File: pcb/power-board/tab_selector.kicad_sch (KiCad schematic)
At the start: 4 parts, among them K20 FINDER-40.41, K21 FINDER-40.41

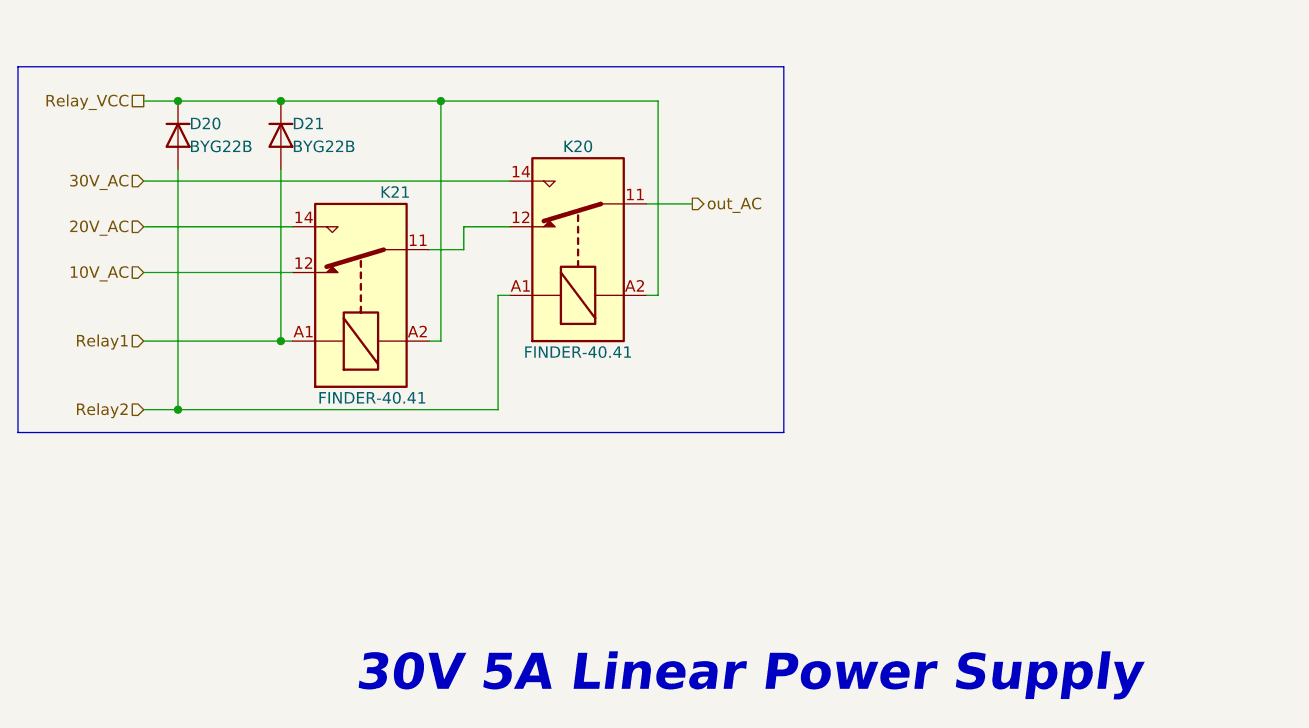
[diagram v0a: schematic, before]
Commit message: Perform minor stylistic changes on power-board schematic, clear DRC
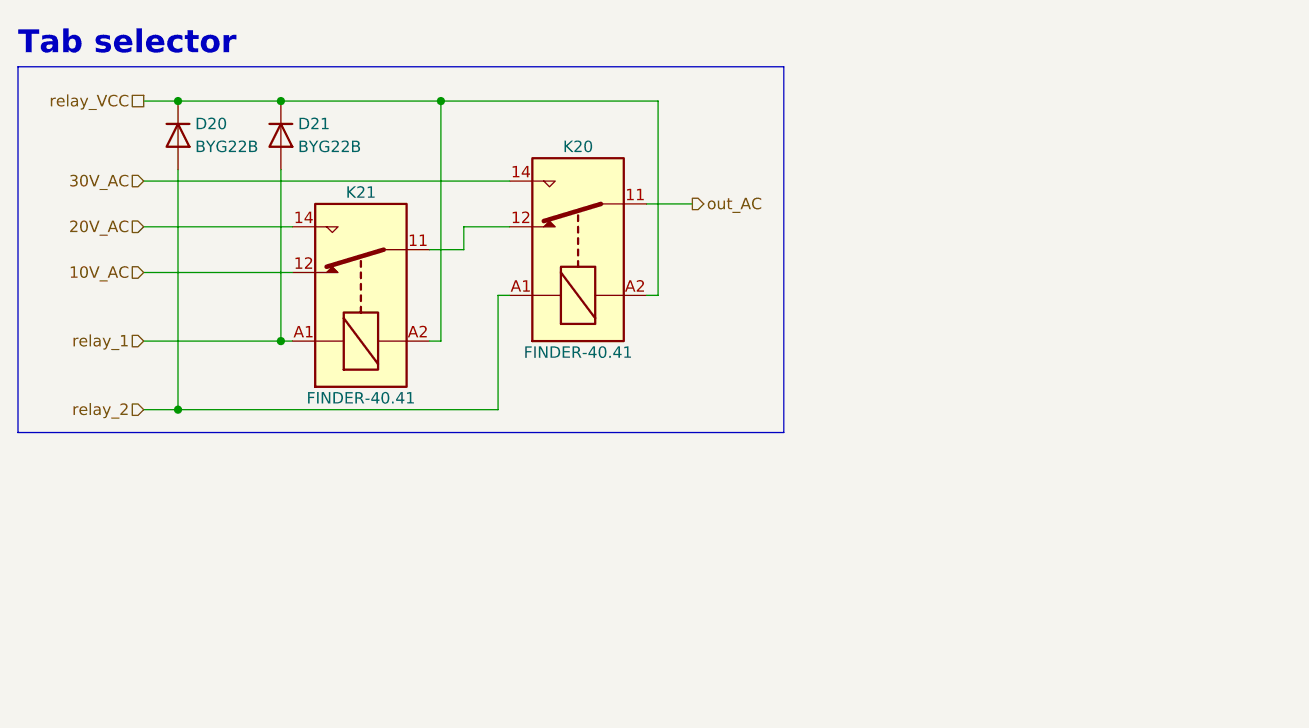
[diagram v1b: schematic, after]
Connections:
- net Relay1 renamed relay_1
- net Relay2 renamed relay_2
- net Relay_VCC renamed relay_VCC
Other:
- note added: "Tab selector"
- note removed: "30V 5A Linear Power Supply"
- title: Tab selector -> DW3005T-power-board
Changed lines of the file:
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@@
 	(paper "A5")
 	(title_block
-		(title "Tab selector")
-		(date "2024-02-24")
-		(rev "V1.0")
+		(title "DW3005T-power-board")
+		(date "2024-02-26")
+		(rev "1.0.0")
 		(company "Dominik Workshop")
 	)
@@
 		)
 	)
-	(text "30V 5A Linear Power Supply"
+	(text "Tab selector"
 		(exclude_from_sim no)
-		(at 95.885 114.3 0)
-		(effects
-			(font
-				(size 4 4)
-				(thickness 0.8)
+		(at 58.42 41.91 0)
+		(effects
+			(font
+				(size 2.54 2.54)
+				(thickness 0.508)
 				(bold yes)
-				(italic yes)
-			)
-			(justify left bottom)
+			)
+			(justify left)
 		)
 	)
@@
 		)
 	)
-	(hierarchical_label "Relay_VCC"
+	(hierarchical_label "relay_VCC"
 		(shape passive)
 		(at 72.39 48.26 180)
@@
 		)
 	)
-	(hierarchical_label "Relay2"
+	(hierarchical_label "relay_2"
 		(shape input)
 		(at 72.39 82.55 180)
@@
 		)
 	)
-	(hierarchical_label "Relay1"
+	(hierarchical_label "relay_1"
 		(shape input)
 		(at 72.39 74.93 180)
@@
 		(dnp no)
 		(property "Reference" "D21"
-			(at 88.9 50.8 90)
+			(at 89.535 50.8 90)
 			(effects
 				(font
@@
 		)
 		(property "Value" "BYG22B"
-			(at 88.9 53.34 90)
+			(at 89.535 53.34 90)
 			(effects
 				(font
@@
 		(dnp no)
 		(property "Reference" "D20"
-			(at 77.47 50.8 90)
+			(at 78.105 50.8 90)
 			(effects
 				(font
@@
 		)
 		(property "Value" "BYG22B"
-			(at 77.47 53.34 90)
+			(at 78.105 53.34 90)
 			(effects
 				(font
@@
 		(dnp no)
 		(property "Reference" "K21"
-			(at 100.33 58.42 90)
+			(at 96.52 58.42 90)
 			(effects
 				(font
@@
 		)
 		(property "Value" "FINDER-40.41"
-			(at 97.79 81.28 90)
-			(effects
-				(font
+			(at 96.52 81.28 90)
+			(effects
+				(font
